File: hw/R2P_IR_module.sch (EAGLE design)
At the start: 32 parts, among them U1 STM32F103CX, U5 LD3985XX, X1 MICROMATCH-4

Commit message: Ongoing board layout
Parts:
- added JP3, JP4, JP5, JP6: (no value), misc:PINHD-1X3
- added U$2, U$3, U$5, U$6: JST-PH3, jst:JST-PH3
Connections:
- new net +VBUS: 1.1, 1.2, 1.3, 2.1, 2.2, 2.3, JP1.1, JP2.1, R4.2, X1-1.S
- new net N$6: JP4.2, U$3.2
- new net N$7: JP6.2, U$6.2
- new net N$8: JP5.2, U$5.2
- net +5V: now also C7.1, JP3.1, JP4.1, JP5.1, JP6.1, R4.1, U$2.1, U$3.1, U$5.1, U$6.1, U5.INHIBIT, U5.VIN; no longer 1.1, 1.2, 1.3, 2.1, 2.2, 2.3, JP1.1, JP2.1, R4.2, X1-1.S
- net GND: now also JP3.3, JP4.3, JP5.3, JP6.3, U$2.3, U$3.3, U$5.3, U$6.3
- net N$5: now also JP3.2, U$2.2; no longer C7.1, R4.1, U5.INHIBIT, U5.VIN
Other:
- moved on the sheet: R4

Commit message: Board layout complete
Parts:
- added R5, R6, R7, R8: (no value), rcl:R-EU_R0603
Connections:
- net +VBUS renamed +V
- removed net AM_DRDY: U1.PB5
- removed net AM_INT1: U1.PB6
- removed net AM_INT2: U1.PB7
- removed net GPS_RESET: U1.PA4
- removed net GPS_RX: U1.PA3
- removed net GPS_STATUS: U1.PA1
- removed net GPS_TX: U1.PA2
- removed net GYRO_CS: U1.PB0
- removed net GYRO_INT1: U1.PB10
- removed net GYRO_INT2: U1.PB1
- removed net MISO: U1.PA6
- removed net MOSI: U1.PA7
- removed net N$1: U$4.P$5
- removed net OSC_OUT: U1.PD1/OSC_OUT
- removed net SCK: U1.PA5
- removed net SCL: U1.PB8
- removed net SDA: U1.PB9
- new net IR1: R5.1, U1.PA1
- new net IR2: R6.1, U1.PA2
- new net IR3: R7.1, U1.PB1
- new net IR4: R8.1, U1.PB0
- net GND: now also U$4.P$5
- net N$5: now also R5.2
- net N$6: now also R6.2
- net N$7: now also R8.2
- net N$8: now also R7.2
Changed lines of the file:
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@@
 <part name="P+2" library="supply" deviceset="+V" device=""/>
 <part name="P+5" library="supply" deviceset="+V" device=""/>
+<part name="R5" library="rcl" deviceset="R-EU_" device="R0603"/>
+<part name="R6" library="rcl" deviceset="R-EU_" device="R0603"/>
+<part name="R7" library="rcl" deviceset="R-EU_" device="R0603"/>
+<part name="R8" library="rcl" deviceset="R-EU_" device="R0603"/>
 </parts>
 <sheets>
@@
 <instance part="P+2" gate="1" x="101.6" y="43.18"/>
 <instance part="P+5" gate="1" x="218.44" y="83.82"/>
+<instance part="R5" gate="G$1" x="190.5" y="226.06"/>
+<instance part="R6" gate="G$1" x="190.5" y="198.12"/>
+<instance part="R7" gate="G$1" x="243.84" y="226.06"/>
+<instance part="R8" gate="G$1" x="243.84" y="198.12"/>
 </instances>
 <busses>
@@
 </segment>
 <segment>
-<wire x1="25.4" y1="78.74" x2="20.32" y2="78.74" width="0.1524" layer="91"/>
+<wire x1="25.4" y1="78.74" x2="22.86" y2="78.74" width="0.1524" layer="91"/>
 <pinref part="U$4" gate="G$1" pin="P$3"/>
 <pinref part="GND2" gate="1" pin="GND"/>
+<wire x1="22.86" y1="78.74" x2="20.32" y2="78.74" width="0.1524" layer="91"/>
+<wire x1="25.4" y1="76.2" x2="22.86" y2="76.2" width="0.1524" layer="91"/>
+<wire x1="22.86" y1="76.2" x2="22.86" y2="78.74" width="0.1524" layer="91"/>
+<pinref part="U$4" gate="G$1" pin="P$5"/>
+<junction x="22.86" y="78.74"/>
 </segment>
 <segment>
@@
 <wire x1="99.06" y1="243.84" x2="106.68" y2="243.84" width="0.1524" layer="91"/>
 <junction x="106.68" y="243.84"/>
+<junction x="121.92" y="243.84"/>
 </segment>
 <segment>
@@
 </segment>
 </net>
-<net name="OSC_OUT" class="0">
-<segment>
-<wire x1="48.26" y1="236.22" x2="48.26" y2="238.76" width="0.1524" layer="91"/>
-<label x="48.26" y="238.76" size="1.778" layer="95" rot="R90"/>
-<pinref part="U1" gate="G$1" pin="PD1/OSC_OUT"/>
-</segment>
-</net>
 <net name="NRST" class="0">
 <segment>
@@
 <label x="45.72" y="71.12" size="1.778" layer="95"/>
 <pinref part="U$4" gate="G$1" pin="P$10"/>
-</segment>
-</net>
-<net name="N$1" class="0">
-<segment>
-<wire x1="25.4" y1="76.2" x2="22.86" y2="76.2" width="0.1524" layer="91"/>
-<wire x1="22.86" y1="76.2" x2="22.86" y2="78.74" width="0.1524" layer="91"/>
-<pinref part="U$4" gate="G$1" pin="P$5"/>
-</segment>
-</net>
-<net name="SCK" class="0">
-<segment>
-<wire x1="43.18" y1="177.8" x2="43.18" y2="175.26" width="0.1524" layer="91"/>
-<label x="43.18" y="170.18" size="1.778" layer="95" rot="R90"/>
-<pinref part="U1" gate="G$1" pin="PA5"/>
-</segment>
-</net>
-<net name="MISO" class="0">
-<segment>
-<wire x1="45.72" y1="177.8" x2="45.72" y2="175.26" width="0.1524" layer="91"/>
-<label x="45.72" y="170.18" size="1.778" layer="95" rot="R90"/>
-<pinref part="U1" gate="G$1" pin="PA6"/>
-</segment>
-</net>
-<net name="MOSI" class="0">
-<segment>
-<wire x1="48.26" y1="177.8" x2="48.26" y2="175.26" width="0.1524" layer="91"/>
-<label x="48.26" y="170.18" size="1.778" layer="95" rot="R90"/>
-<pinref part="U1" gate="G$1" pin="PA7"/>
 </segment>
 </net>
@@
 </segment>
 </net>
-<net name="GYRO_CS" class="0">
-<segment>
-<pinref part="U1" gate="G$1" pin="PB0"/>
-<wire x1="83.82" y1="193.04" x2="86.36" y2="193.04" width="0.1524" layer="91"/>
-<label x="86.36" y="193.04" size="1.778" layer="95"/>
-</segment>
-</net>
-<net name="GYRO_INT1" class="0">
-<segment>
-<wire x1="83.82" y1="218.44" x2="86.36" y2="218.44" width="0.1524" layer="91"/>
-<label x="86.36" y="218.44" size="1.778" layer="95"/>
-<pinref part="U1" gate="G$1" pin="PB10"/>
-</segment>
-</net>
-<net name="GYRO_INT2" class="0">
-<segment>
-<wire x1="83.82" y1="195.58" x2="86.36" y2="195.58" width="0.1524" layer="91"/>
-<label x="86.36" y="195.58" size="1.778" layer="95"/>
-<pinref part="U1" gate="G$1" pin="PB1"/>
-</segment>
-</net>
 <net name="N$4" class="0">
 <segment>
@@
 <pinref part="SOT1" gate="G$1" pin="RS"/>
 <pinref part="R1" gate="G$1" pin="1"/>
-</segment>
-</net>
-<net name="SCL" class="0">
-<segment>
-<wire x1="83.82" y1="213.36" x2="86.36" y2="213.36" width="0.1524" layer="91"/>
-<label x="86.36" y="213.36" size="1.778" layer="95"/>
-<pinref part="U1" gate="G$1" pin="PB8"/>
-</segment>
-</net>
-<net name="SDA" class="0">
-<segment>
-<wire x1="83.82" y1="215.9" x2="86.36" y2="215.9" width="0.1524" layer="91"/>
-<label x="86.36" y="215.9" size="1.778" layer="95"/>
-<pinref part="U1" gate="G$1" pin="PB9"/>
-</segment>
-</net>
-<net name="AM_INT1" class="0">
-<segment>
-<wire x1="83.82" y1="208.28" x2="86.36" y2="208.28" width="0.1524" layer="91"/>
-<label x="86.36" y="208.28" size="1.778" layer="95"/>
-<pinref part="U1" gate="G$1" pin="PB6"/>
-</segment>
-</net>
-<net name="AM_DRDY" class="0">
-<segment>
-<wire x1="83.82" y1="205.74" x2="86.36" y2="205.74" width="0.1524" layer="91"/>
-<label x="86.36" y="205.74" size="1.778" layer="95"/>
-<pinref part="U1" gate="G$1" pin="PB5"/>
-</segment>
-</net>
-<net name="AM_INT2" class="0">
-<segment>
-<wire x1="83.82" y1="210.82" x2="86.36" y2="210.82" width="0.1524" layer="91"/>
-<label x="86.36" y="210.82" size="1.778" layer="95"/>
-<pinref part="U1" gate="G$1" pin="PB7"/>
-</segment>
-</net>
-<net name="GPS_TX" class="0">
-<segment>
-<wire x1="25.4" y1="195.58" x2="22.86" y2="195.58" width="0.1524" layer="91"/>
-<label x="15.24" y="195.58" size="1.778" layer="95"/>
-<pinref part="U1" gate="G$1" pin="PA2"/>
-</segment>
-</net>
-<net name="GPS_RX" class="0">
-<segment>
-<wire x1="25.4" y1="193.04" x2="22.86" y2="193.04" width="0.1524" layer="91"/>
-<label x="15.24" y="193.04" size="1.778" layer="95"/>
-<pinref part="U1" gate="G$1" pin="PA3"/>
-</segment>
-</net>
-<net name="GPS_RESET" class="0">
-<segment>
-<wire x1="40.64" y1="177.8" x2="40.64" y2="175.26" width="0.1524" layer="91"/>
-<label x="40.64" y="162.56" size="1.778" layer="95" rot="R90"/>
-<pinref part="U1" gate="G$1" pin="PA4"/>
-</segment>
-</net>
-<net name="GPS_STATUS" class="0">
-<segment>
-<wire x1="25.4" y1="198.12" x2="22.86" y2="198.12" width="0.1524" layer="91"/>
-<label x="15.24" y="198.12" size="1.778" layer="95"/>
-<pinref part="U1" gate="G$1" pin="PA1"/>
 </segment>
 </net>
@@
 <pinref part="P+10" gate="1" pin="+5V"/>
 <wire x1="81.28" y1="137.16" x2="81.28" y2="134.62" width="0.1524" layer="91"/>
-</segment>
-</net>
-<net name="+VBUS" class="0">
+<junction x="81.28" y="134.62"/>
+</segment>
+</net>
+<net name="+V" class="0">
 <segment>
 <pinref part="R4" gate="G$1" pin="2"/>
@@
 <pinref part="JP3" gate="A" pin="2"/>
 <wire x1="210.82" y1="226.06" x2="220.98" y2="226.06" width="0.1524" layer="91"/>
+<pinref part="R5" gate="G$1" pin="2"/>
+<wire x1="210.82" y1="226.06" x2="195.58" y2="226.06" width="0.1524" layer="91"/>
+<junction x="210.82" y="226.06"/>
 </segment>
 </net>
@@
 <pinref part="JP4" gate="A" pin="2"/>
 <wire x1="210.82" y1="198.12" x2="220.98" y2="198.12" width="0.1524" layer="91"/>
+<pinref part="R6" gate="G$1" pin="2"/>
+<wire x1="210.82" y1="198.12" x2="195.58" y2="198.12" width="0.1524" layer="91"/>
+<junction x="210.82" y="198.12"/>
 </segment>
 </net>
@@
 <pinref part="JP6" gate="A" pin="2"/>
 <wire x1="264.16" y1="198.12" x2="274.32" y2="198.12" width="0.1524" layer="91"/>
+<pinref part="R8" gate="G$1" pin="2"/>
+<wire x1="264.16" y1="198.12" x2="248.92" y2="198.12" width="0.1524" layer="91"/>
+<junction x="264.16" y="198.12"/>
 </segment>
 </net>
@@
 <pinref part="JP5" gate="A" pin="2"/>
 <wire x1="264.16" y1="226.06" x2="274.32" y2="226.06" width="0.1524" layer="91"/>
-</segment>
-</net>
+<pinref part="R7" gate="G$1" pin="2"/>
+<wire x1="264.16" y1="226.06" x2="248.92" y2="226.06" width="0.1524" layer="91"/>
+<junction x="264.16" y="226.06"/>
+</segment>
+</net>
+<net name="IR2" class="0">
+<segment>
+<pinref part="R6" gate="G$1" pin="1"/>
+<wire x1="185.42" y1="198.12" x2="180.34" y2="198.12" width="0.1524" layer="91"/>
+<label x="175.26" y="198.12" size="1.778" layer="95"/>
+</segment>
+<segment>
+<wire x1="25.4" y1="195.58" x2="22.86" y2="195.58" width="0.1524" layer="91"/>
+<label x="15.24" y="195.58" size="1.778" layer="95"/>
+<pinref part="U1" gate="G$1" pin="PA2"/>
+</segment>
+</net>
+<net name="IR1" class="0">
+<segment>
+<pinref part="R5" gate="G$1" pin="1"/>
+<wire x1="185.42" y1="226.06" x2="180.34" y2="226.06" width="0.1524" layer="91"/>
+<label x="175.26" y="226.06" size="1.778" layer="95"/>
+</segment>
+<segment>
+<wire x1="25.4" y1="198.12" x2="22.86" y2="198.12" width="0.1524" layer="91"/>
+<label x="15.24" y="198.12" size="1.778" layer="95"/>
+<pinref part="U1" gate="G$1" pin="PA1"/>
+</segment>
+</net>
+<net name="IR3" class="0">
+<segment>
+<pinref part="R7" gate="G$1" pin="1"/>
+<wire x1="238.76" y1="226.06" x2="233.68" y2="226.06" width="0.1524" layer="91"/>
+<label x="228.6" y="226.06" size="1.778" layer="95"/>
+</segment>
+<segment>
+<pinref part="U1" gate="G$1" pin="PB1"/>
+<wire x1="83.82" y1="195.58" x2="86.36" y2="195.58" width="0.1524" layer="91"/>
+<label x="86.36" y="195.58" size="1.778" layer="95"/>
+</segment>
+</net>
+<net name="IR4" class="0">
+<segment>
+<pinref part="R8" gate="G$1" pin="1"/>
+<wire x1="238.76" y1="198.12" x2="233.68" y2="198.12" width="0.1524" layer="91"/>
+<label x="228.6" y="198.12" size="1.778" layer="95"/>
+</segment>
+<segment>
+<pinref part="U1" gate="G$1" pin="PB0"/>
+<wire x1="83.82" y1="193.04" x2="86.36" y2="193.04" width="0.1524" layer="91"/>
+<label x="86.36" y="193.04" size="1.778" layer="95"/>
+</segment>
+</net>

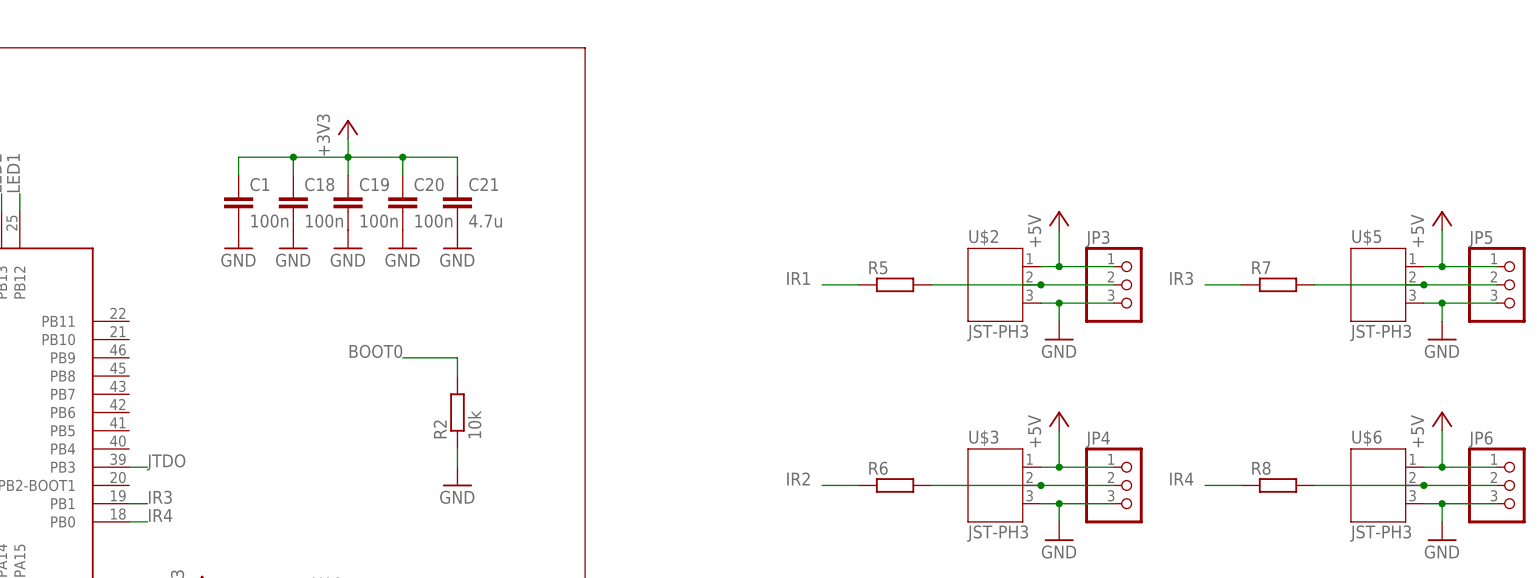
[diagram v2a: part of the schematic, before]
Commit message: Added PMOS to shut down IR sensors
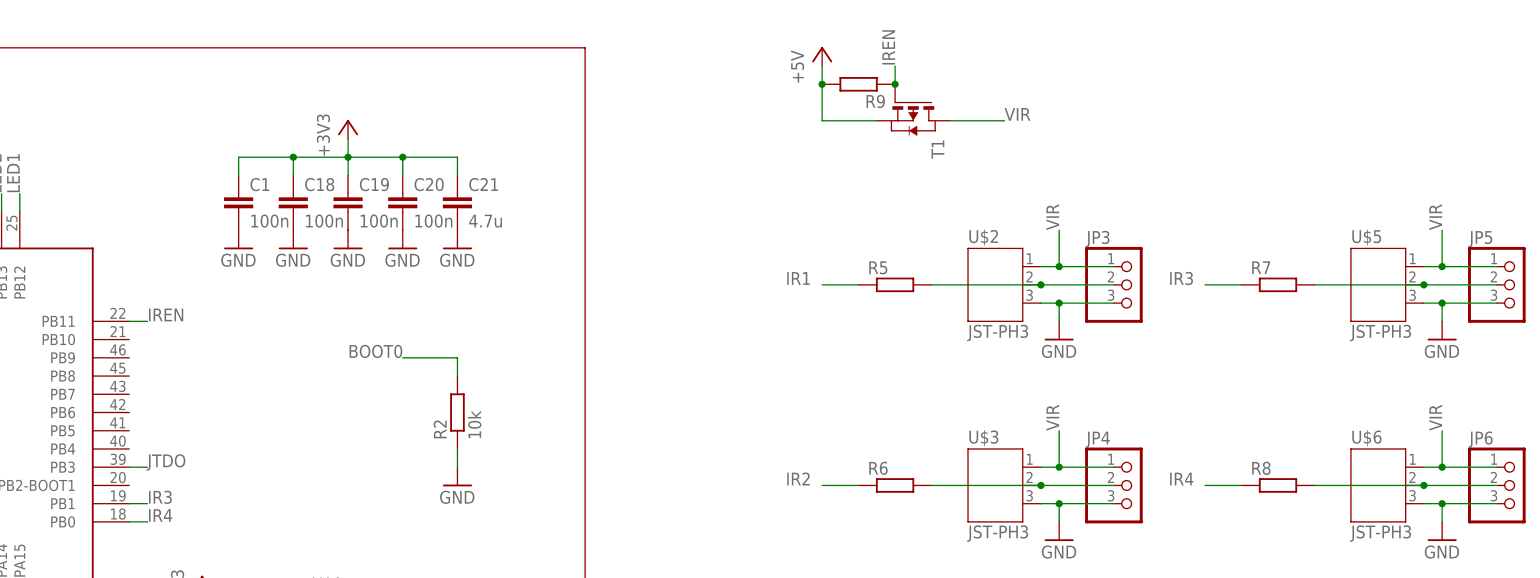
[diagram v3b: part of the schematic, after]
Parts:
- added R9: (no value), rcl:R-EU_R0603
- added T1: (no value), zetex:PMOSSOT23
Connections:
- new net IREN: R9.1, T1.G, U1.PB11
- new net VIR: JP3.1, JP4.1, JP5.1, JP6.1, T1.D, U$2.1, U$3.1, U$5.1, U$6.1
- net +5V: now also R9.2, T1.S; no longer JP3.1, JP4.1, JP5.1, JP6.1, U$2.1, U$3.1, U$5.1, U$6.1
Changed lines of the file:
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@@
 <part name="GND20" library="supply1" deviceset="GND" device=""/>
 <part name="P+3" library="supply" deviceset="+5V" device=""/>
-<part name="P+6" library="supply" deviceset="+5V" device=""/>
-<part name="P+7" library="supply" deviceset="+5V" device=""/>
-<part name="P+8" library="supply" deviceset="+5V" device=""/>
 <part name="P+9" library="supply" deviceset="+V" device=""/>
 <part name="P+10" library="supply" deviceset="+5V" device=""/>
@@
 <part name="R7" library="rcl" deviceset="R-EU_" device="R0603"/>
 <part name="R8" library="rcl" deviceset="R-EU_" device="R0603"/>
+<part name="T1" library="zetex" deviceset="PMOSSOT23" device=""/>
+<part name="R9" library="rcl" deviceset="R-EU_" device="R0603"/>
 </parts>
 <sheets>
@@
 <instance part="GND14" gate="1" x="266.7" y="190.5"/>
 <instance part="GND20" gate="1" x="213.36" y="190.5"/>
-<instance part="P+3" gate="1" x="213.36" y="236.22"/>
-<instance part="P+6" gate="1" x="266.7" y="236.22"/>
-<instance part="P+7" gate="1" x="266.7" y="208.28"/>
-<instance part="P+8" gate="1" x="213.36" y="208.28"/>
+<instance part="P+3" gate="1" x="180.34" y="259.08"/>
 <instance part="P+9" gate="1" x="83.82" y="106.68"/>
 <instance part="P+10" gate="1" x="81.28" y="139.7"/>
@@
 <instance part="R7" gate="G$1" x="243.84" y="226.06"/>
 <instance part="R8" gate="G$1" x="243.84" y="198.12"/>
+<instance part="T1" gate="A" x="193.04" y="248.92" rot="R270"/>
+<instance part="R9" gate="G$1" x="185.42" y="254" rot="R180"/>
 </instances>
 <busses>
@@
 <net name="+5V" class="0">
 <segment>
-<pinref part="U$2" gate="G$1" pin="1"/>
-<wire x1="210.82" y1="228.6" x2="213.36" y2="228.6" width="0.1524" layer="91"/>
-<wire x1="213.36" y1="228.6" x2="213.36" y2="233.68" width="0.1524" layer="91"/>
-<pinref part="P+3" gate="1" pin="+5V"/>
-<pinref part="JP3" gate="A" pin="1"/>
-<wire x1="220.98" y1="228.6" x2="213.36" y2="228.6" width="0.1524" layer="91"/>
-<junction x="213.36" y="228.6"/>
-</segment>
-<segment>
-<pinref part="U$5" gate="G$1" pin="1"/>
-<wire x1="264.16" y1="228.6" x2="266.7" y2="228.6" width="0.1524" layer="91"/>
-<wire x1="266.7" y1="228.6" x2="266.7" y2="233.68" width="0.1524" layer="91"/>
-<pinref part="P+6" gate="1" pin="+5V"/>
-<pinref part="JP5" gate="A" pin="1"/>
-<wire x1="274.32" y1="228.6" x2="266.7" y2="228.6" width="0.1524" layer="91"/>
-<junction x="266.7" y="228.6"/>
-</segment>
-<segment>
-<pinref part="U$6" gate="G$1" pin="1"/>
-<wire x1="264.16" y1="200.66" x2="266.7" y2="200.66" width="0.1524" layer="91"/>
-<wire x1="266.7" y1="200.66" x2="266.7" y2="205.74" width="0.1524" layer="91"/>
-<pinref part="P+7" gate="1" pin="+5V"/>
-<pinref part="JP6" gate="A" pin="1"/>
-<wire x1="274.32" y1="200.66" x2="266.7" y2="200.66" width="0.1524" layer="91"/>
-<junction x="266.7" y="200.66"/>
-</segment>
-<segment>
-<pinref part="U$3" gate="G$1" pin="1"/>
-<wire x1="210.82" y1="200.66" x2="213.36" y2="200.66" width="0.1524" layer="91"/>
-<wire x1="213.36" y1="200.66" x2="213.36" y2="205.74" width="0.1524" layer="91"/>
-<pinref part="P+8" gate="1" pin="+5V"/>
-<pinref part="JP4" gate="A" pin="1"/>
-<wire x1="220.98" y1="200.66" x2="213.36" y2="200.66" width="0.1524" layer="91"/>
-<junction x="213.36" y="200.66"/>
-</segment>
-<segment>
 <pinref part="R4" gate="G$1" pin="1"/>
 <pinref part="P+4" gate="1" pin="+5V"/>
@@
 <wire x1="81.28" y1="137.16" x2="81.28" y2="134.62" width="0.1524" layer="91"/>
 <junction x="81.28" y="134.62"/>
+</segment>
+<segment>
+<pinref part="T1" gate="A" pin="S"/>
+<pinref part="P+3" gate="1" pin="+5V"/>
+<wire x1="187.96" y1="248.92" x2="180.34" y2="248.92" width="0.1524" layer="91"/>
+<wire x1="180.34" y1="248.92" x2="180.34" y2="254" width="0.1524" layer="91"/>
+<pinref part="R9" gate="G$1" pin="2"/>
+<wire x1="180.34" y1="254" x2="180.34" y2="256.54" width="0.1524" layer="91"/>
+<junction x="180.34" y="254"/>
 </segment>
 </net>
@@
 </segment>
 </net>
+<net name="VIR" class="0">
+<segment>
+<pinref part="T1" gate="A" pin="D"/>
+<wire x1="198.12" y1="248.92" x2="205.74" y2="248.92" width="0.1524" layer="91"/>
+<label x="205.74" y="248.92" size="1.778" layer="95"/>
+</segment>
+<segment>
+<pinref part="U$2" gate="G$1" pin="1"/>
+<wire x1="210.82" y1="228.6" x2="213.36" y2="228.6" width="0.1524" layer="91"/>
+<pinref part="JP3" gate="A" pin="1"/>
+<wire x1="220.98" y1="228.6" x2="213.36" y2="228.6" width="0.1524" layer="91"/>
+<wire x1="213.36" y1="228.6" x2="213.36" y2="233.68" width="0.1524" layer="91"/>
+<junction x="213.36" y="228.6"/>
+<label x="213.36" y="233.68" size="1.778" layer="95" rot="R90"/>
+</segment>
+<segment>
+<pinref part="U$5" gate="G$1" pin="1"/>
+<wire x1="264.16" y1="228.6" x2="266.7" y2="228.6" width="0.1524" layer="91"/>
+<pinref part="JP5" gate="A" pin="1"/>
+<wire x1="274.32" y1="228.6" x2="266.7" y2="228.6" width="0.1524" layer="91"/>
+<wire x1="266.7" y1="228.6" x2="266.7" y2="233.68" width="0.1524" layer="91"/>
+<junction x="266.7" y="228.6"/>
+<label x="266.7" y="233.68" size="1.778" layer="95" rot="R90"/>
+</segment>
+<segment>
+<pinref part="U$6" gate="G$1" pin="1"/>
+<wire x1="264.16" y1="200.66" x2="266.7" y2="200.66" width="0.1524" layer="91"/>
+<pinref part="JP6" gate="A" pin="1"/>
+<wire x1="274.32" y1="200.66" x2="266.7" y2="200.66" width="0.1524" layer="91"/>
+<wire x1="266.7" y1="200.66" x2="266.7" y2="205.74" width="0.1524" layer="91"/>
+<junction x="266.7" y="200.66"/>
+<label x="266.7" y="205.74" size="1.778" layer="95" rot="R90"/>
+</segment>
+<segment>
+<pinref part="U$3" gate="G$1" pin="1"/>
+<wire x1="210.82" y1="200.66" x2="213.36" y2="200.66" width="0.1524" layer="91"/>
+<pinref part="JP4" gate="A" pin="1"/>
+<wire x1="220.98" y1="200.66" x2="213.36" y2="200.66" width="0.1524" layer="91"/>
+<wire x1="213.36" y1="200.66" x2="213.36" y2="205.74" width="0.1524" layer="91"/>
+<junction x="213.36" y="200.66"/>
+<label x="213.36" y="205.74" size="1.778" layer="95" rot="R90"/>
+</segment>
+</net>
+<net name="IREN" class="0">
+<segment>
+<pinref part="T1" gate="A" pin="G"/>
+<wire x1="190.5" y1="254" x2="190.5" y2="256.54" width="0.1524" layer="91"/>
+<label x="190.5" y="256.54" size="1.778" layer="95" rot="R90"/>
+<pinref part="R9" gate="G$1" pin="1"/>
+<junction x="190.5" y="254"/>
+</segment>
+<segment>
+<pinref part="U1" gate="G$1" pin="PB11"/>
+<wire x1="83.82" y1="220.98" x2="86.36" y2="220.98" width="0.1524" layer="91"/>
+<label x="86.36" y="220.98" size="1.778" layer="95"/>
+</segment>
+</net>
